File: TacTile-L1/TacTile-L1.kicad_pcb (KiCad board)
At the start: 2 copper layers, 25 x 60 mm, 10 parts, among them J1 Conn_01x02, J2 Conn_01x02

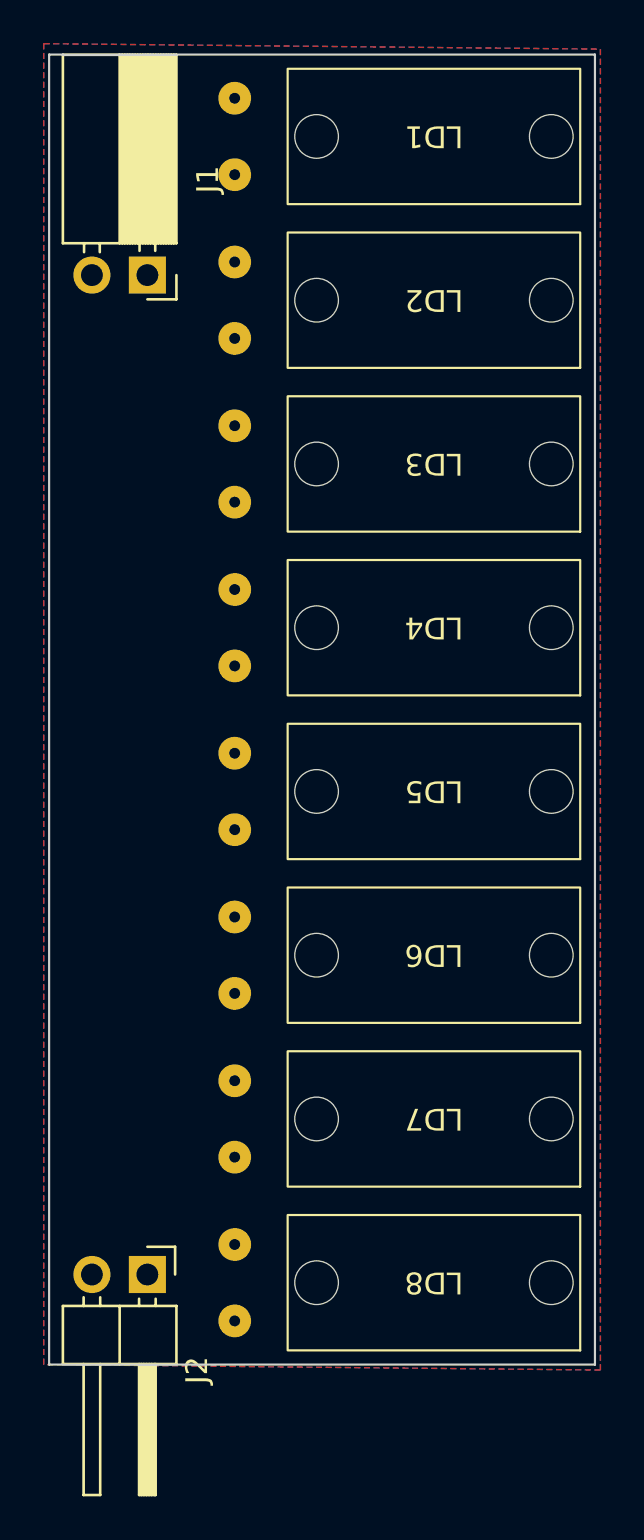
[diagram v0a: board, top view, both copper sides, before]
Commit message: Adjusted mounting for laser boards
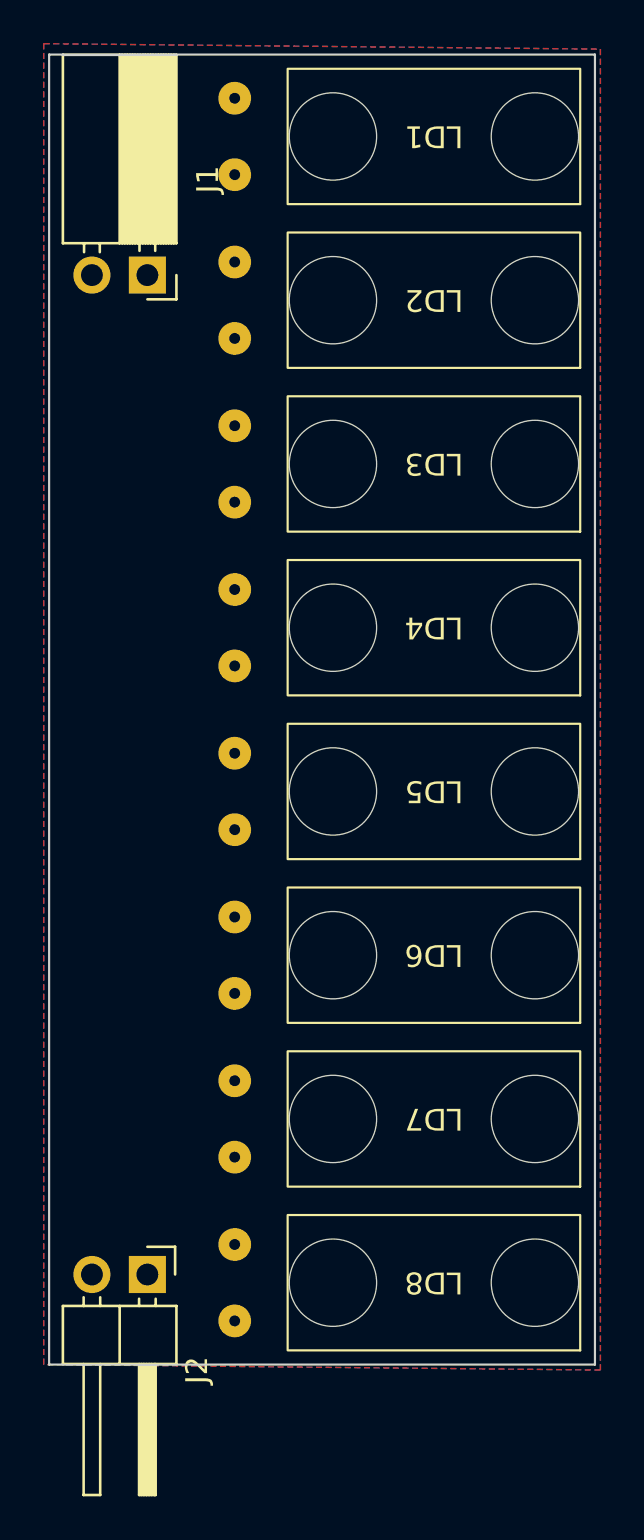
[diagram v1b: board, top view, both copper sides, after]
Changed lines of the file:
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@@
     (fp_rect (start -13.325 -3.1) (end 0.075 3.1)
       (stroke (width 0.1) (type default)) (fill none) (layer "F.SilkS"))
-    (fp_rect (start -13.75 -3.75) (end 0.5 3.75)
-      (stroke (width 0.05) (type default)) (fill none) (layer "F.CrtYd"))
-    (fp_rect (start -13.25 -3) (end 0 3)
-      (stroke (width 0.1) (type default)) (fill none) (layer "F.Fab"))
-    (pad "" np_thru_hole circle (at -12 0 180) (size 2 2) (drill 2) (layers "F&B.Cu" "*.Mask"))
-    (pad "" np_thru_hole circle (at -1.25 0 180) (size 2 2) (drill 2) (layers "F&B.Cu" "*.Mask"))
+    (fp_rect (start -13.25 -3.75) (end 0 3.75)
+      (stroke (width 0.05) (type default)) (fill none) (layer "F.CrtYd"))
+    (fp_rect (start -13.25 -3) (end 0 3)
+      (stroke (width 0.1) (type default)) (fill none) (layer "F.Fab"))
+    (pad "" np_thru_hole circle (at -11.25 0 180) (size 4 4) (drill 4) (layers "F&B.Cu" "*.Mask"))
+    (pad "" np_thru_hole circle (at -2 0 180) (size 4 4) (drill 4) (layers "F&B.Cu" "*.Mask"))
     (pad "1" thru_hole circle (at 2.5 -1.75 180) (size 1.5 1.5) (drill 0.5) (layers "*.Cu" "*.Mask")
       (net 2 "/GND") (pinfunction "K") (pintype "passive"))
@@
     (fp_rect (start -13.325 -3.1) (end 0.075 3.1)
       (stroke (width 0.1) (type default)) (fill none) (layer "F.SilkS"))
-    (fp_rect (start -13.75 -3.75) (end 0.5 3.75)
-      (stroke (width 0.05) (type default)) (fill none) (layer "F.CrtYd"))
-    (fp_rect (start -13.25 -3) (end 0 3)
-      (stroke (width 0.1) (type default)) (fill none) (layer "F.Fab"))
-    (pad "" np_thru_hole circle (at -12 0 180) (size 2 2) (drill 2) (layers "F&B.Cu" "*.Mask"))
-    (pad "" np_thru_hole circle (at -1.25 0 180) (size 2 2) (drill 2) (layers "F&B.Cu" "*.Mask"))
+    (fp_rect (start -13.25 -3.75) (end 0 3.75)
+      (stroke (width 0.05) (type default)) (fill none) (layer "F.CrtYd"))
+    (fp_rect (start -13.25 -3) (end 0 3)
+      (stroke (width 0.1) (type default)) (fill none) (layer "F.Fab"))
+    (pad "" np_thru_hole circle (at -11.25 0 180) (size 4 4) (drill 4) (layers "F&B.Cu" "*.Mask"))
+    (pad "" np_thru_hole circle (at -2 0 180) (size 4 4) (drill 4) (layers "F&B.Cu" "*.Mask"))
     (pad "1" thru_hole circle (at 2.5 -1.75 180) (size 1.5 1.5) (drill 0.5) (layers "*.Cu" "*.Mask")
       (net 2 "/GND") (pinfunction "K") (pintype "passive"))
@@
     (fp_rect (start -13.325 -3.1) (end 0.075 3.1)
       (stroke (width 0.1) (type default)) (fill none) (layer "F.SilkS"))
-    (fp_rect (start -13.75 -3.75) (end 0.5 3.75)
-      (stroke (width 0.05) (type default)) (fill none) (layer "F.CrtYd"))
-    (fp_rect (start -13.25 -3) (end 0 3)
-      (stroke (width 0.1) (type default)) (fill none) (layer "F.Fab"))
-    (pad "" np_thru_hole circle (at -12 0 180) (size 2 2) (drill 2) (layers "F&B.Cu" "*.Mask"))
-    (pad "" np_thru_hole circle (at -1.25 0 180) (size 2 2) (drill 2) (layers "F&B.Cu" "*.Mask"))
+    (fp_rect (start -13.25 -3.75) (end 0 3.75)
+      (stroke (width 0.05) (type default)) (fill none) (layer "F.CrtYd"))
+    (fp_rect (start -13.25 -3) (end 0 3)
+      (stroke (width 0.1) (type default)) (fill none) (layer "F.Fab"))
+    (pad "" np_thru_hole circle (at -11.25 0 180) (size 4 4) (drill 4) (layers "F&B.Cu" "*.Mask"))
+    (pad "" np_thru_hole circle (at -2 0 180) (size 4 4) (drill 4) (layers "F&B.Cu" "*.Mask"))
     (pad "1" thru_hole circle (at 2.5 -1.75 180) (size 1.5 1.5) (drill 0.5) (layers "*.Cu" "*.Mask")
       (net 2 "/GND") (pinfunction "K") (pintype "passive"))
@@
     (fp_rect (start -13.325 -3.1) (end 0.075 3.1)
       (stroke (width 0.1) (type default)) (fill none) (layer "F.SilkS"))
-    (fp_rect (start -13.75 -3.75) (end 0.5 3.75)
-      (stroke (width 0.05) (type default)) (fill none) (layer "F.CrtYd"))
-    (fp_rect (start -13.25 -3) (end 0 3)
-      (stroke (width 0.1) (type default)) (fill none) (layer "F.Fab"))
-    (pad "" np_thru_hole circle (at -12 0 180) (size 2 2) (drill 2) (layers "F&B.Cu" "*.Mask"))
-    (pad "" np_thru_hole circle (at -1.25 0 180) (size 2 2) (drill 2) (layers "F&B.Cu" "*.Mask"))
+    (fp_rect (start -13.25 -3.75) (end 0 3.75)
+      (stroke (width 0.05) (type default)) (fill none) (layer "F.CrtYd"))
+    (fp_rect (start -13.25 -3) (end 0 3)
+      (stroke (width 0.1) (type default)) (fill none) (layer "F.Fab"))
+    (pad "" np_thru_hole circle (at -11.25 0 180) (size 4 4) (drill 4) (layers "F&B.Cu" "*.Mask"))
+    (pad "" np_thru_hole circle (at -2 0 180) (size 4 4) (drill 4) (layers "F&B.Cu" "*.Mask"))
     (pad "1" thru_hole circle (at 2.5 -1.75 180) (size 1.5 1.5) (drill 0.5) (layers "*.Cu" "*.Mask")
       (net 2 "/GND") (pinfunction "K") (pintype "passive"))
@@
     (fp_rect (start -13.325 -3.1) (end 0.075 3.1)
       (stroke (width 0.1) (type default)) (fill none) (layer "F.SilkS"))
-    (fp_rect (start -13.75 -3.75) (end 0.5 3.75)
-      (stroke (width 0.05) (type default)) (fill none) (layer "F.CrtYd"))
-    (fp_rect (start -13.25 -3) (end 0 3)
-      (stroke (width 0.1) (type default)) (fill none) (layer "F.Fab"))
-    (pad "" np_thru_hole circle (at -12 0 180) (size 2 2) (drill 2) (layers "F&B.Cu" "*.Mask"))
-    (pad "" np_thru_hole circle (at -1.25 0 180) (size 2 2) (drill 2) (layers "F&B.Cu" "*.Mask"))
+    (fp_rect (start -13.25 -3.75) (end 0 3.75)
+      (stroke (width 0.05) (type default)) (fill none) (layer "F.CrtYd"))
+    (fp_rect (start -13.25 -3) (end 0 3)
+      (stroke (width 0.1) (type default)) (fill none) (layer "F.Fab"))
+    (pad "" np_thru_hole circle (at -11.25 0 180) (size 4 4) (drill 4) (layers "F&B.Cu" "*.Mask"))
+    (pad "" np_thru_hole circle (at -2 0 180) (size 4 4) (drill 4) (layers "F&B.Cu" "*.Mask"))
     (pad "1" thru_hole circle (at 2.5 -1.75 180) (size 1.5 1.5) (drill 0.5) (layers "*.Cu" "*.Mask")
       (net 2 "/GND") (pinfunction "K") (pintype "passive"))
@@
     (fp_rect (start -13.325 -3.1) (end 0.075 3.1)
       (stroke (width 0.1) (type default)) (fill none) (layer "F.SilkS"))
-    (fp_rect (start -13.75 -3.75) (end 0.5 3.75)
-      (stroke (width 0.05) (type default)) (fill none) (layer "F.CrtYd"))
-    (fp_rect (start -13.25 -3) (end 0 3)
-      (stroke (width 0.1) (type default)) (fill none) (layer "F.Fab"))
-    (pad "" np_thru_hole circle (at -12 0 180) (size 2 2) (drill 2) (layers "F&B.Cu" "*.Mask"))
-    (pad "" np_thru_hole circle (at -1.25 0 180) (size 2 2) (drill 2) (layers "F&B.Cu" "*.Mask"))
+    (fp_rect (start -13.25 -3.75) (end 0 3.75)
+      (stroke (width 0.05) (type default)) (fill none) (layer "F.CrtYd"))
+    (fp_rect (start -13.25 -3) (end 0 3)
+      (stroke (width 0.1) (type default)) (fill none) (layer "F.Fab"))
+    (pad "" np_thru_hole circle (at -11.25 0 180) (size 4 4) (drill 4) (layers "F&B.Cu" "*.Mask"))
+    (pad "" np_thru_hole circle (at -2 0 180) (size 4 4) (drill 4) (layers "F&B.Cu" "*.Mask"))
     (pad "1" thru_hole circle (at 2.5 -1.75 180) (size 1.5 1.5) (drill 0.5) (layers "*.Cu" "*.Mask")
       (net 2 "/GND") (pinfunction "K") (pintype "passive"))
@@
     (fp_rect (start -13.325 -3.1) (end 0.075 3.1)
       (stroke (width 0.1) (type default)) (fill none) (layer "F.SilkS"))
-    (fp_rect (start -13.75 -3.75) (end 0.5 3.75)
-      (stroke (width 0.05) (type default)) (fill none) (layer "F.CrtYd"))
-    (fp_rect (start -13.25 -3) (end 0 3)
-      (stroke (width 0.1) (type default)) (fill none) (layer "F.Fab"))
-    (pad "" np_thru_hole circle (at -12 0 180) (size 2 2) (drill 2) (layers "F&B.Cu" "*.Mask"))
-    (pad "" np_thru_hole circle (at -1.25 0 180) (size 2 2) (drill 2) (layers "F&B.Cu" "*.Mask"))
+    (fp_rect (start -13.25 -3.75) (end 0 3.75)
+      (stroke (width 0.05) (type default)) (fill none) (layer "F.CrtYd"))
+    (fp_rect (start -13.25 -3) (end 0 3)
+      (stroke (width 0.1) (type default)) (fill none) (layer "F.Fab"))
+    (pad "" np_thru_hole circle (at -11.25 0 180) (size 4 4) (drill 4) (layers "F&B.Cu" "*.Mask"))
+    (pad "" np_thru_hole circle (at -2 0 180) (size 4 4) (drill 4) (layers "F&B.Cu" "*.Mask"))
     (pad "1" thru_hole circle (at 2.5 -1.75 180) (size 1.5 1.5) (drill 0.5) (layers "*.Cu" "*.Mask")
       (net 2 "/GND") (pinfunction "K") (pintype "passive"))
@@
     (fp_rect (start -13.325 -3.1) (end 0.075 3.1)
       (stroke (width 0.1) (type default)) (fill none) (layer "F.SilkS"))
-    (fp_rect (start -13.75 -3.75) (end 0.5 3.75)
-      (stroke (width 0.05) (type default)) (fill none) (layer "F.CrtYd"))
-    (fp_rect (start -13.25 -3) (end 0 3)
-      (stroke (width 0.1) (type default)) (fill none) (layer "F.Fab"))
-    (pad "" np_thru_hole circle (at -12 0 180) (size 2 2) (drill 2) (layers "F&B.Cu" "*.Mask"))
-    (pad "" np_thru_hole circle (at -1.25 0 180) (size 2 2) (drill 2) (layers "F&B.Cu" "*.Mask"))
-    (pad "1" thru_hole circle (at 2.5 -1.75 180) (size 1.5 1.5) (drill 0.5) (layers "*.Cu" "*.Mask")
-      (net 2 "/GND") (pinfunction "K") (pintype "passive"))
+    (fp_rect (start -13.25 -3.75) (end 0 3.75)
+      (stroke (width 0.05) (type default)) (fill none) (layer "F.CrtYd"))
+    (fp_rect (start -13.25 -3) (end 0 3)
+      (stroke (width 0.1) (type default)) (fill none) (layer "F.Fab"))
+    (pad "" np_thru_hole circle (at -11.25 0 180) (size 4 4) (drill 4) (layers "F&B.Cu" "*.Mask"))
+    (pad "" np_thru_hole circle (at -2 0 180) (size 4 4) (drill 4) (layers "F&B.Cu" "*.Mask"))
+    (pad "1" thru_hole circle (at 2.5 -1.75 180) (size 1.5 1.5) (drill 0.5) (layers "*.Cu" "*.Mask")
+      (net 2 "/GND") (pinfunction "K") (pintype "passive"))
